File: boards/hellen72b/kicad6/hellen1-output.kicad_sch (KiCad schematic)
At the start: 56 parts

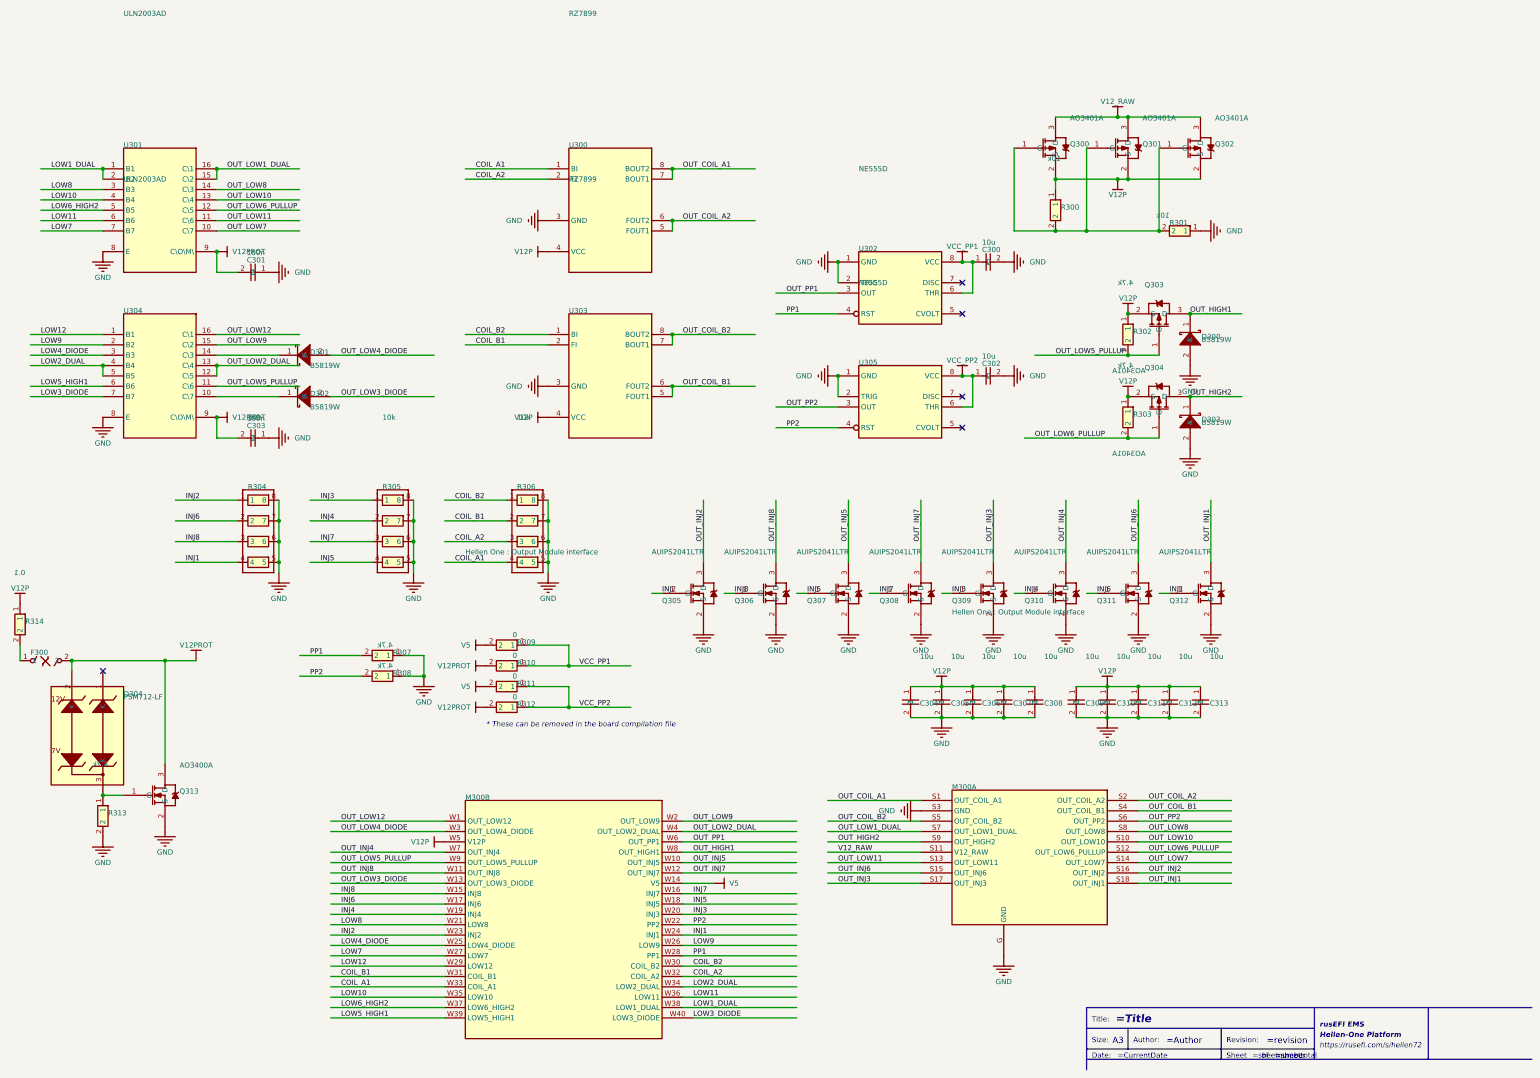
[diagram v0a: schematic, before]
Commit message: update exported kicad files after refactoring
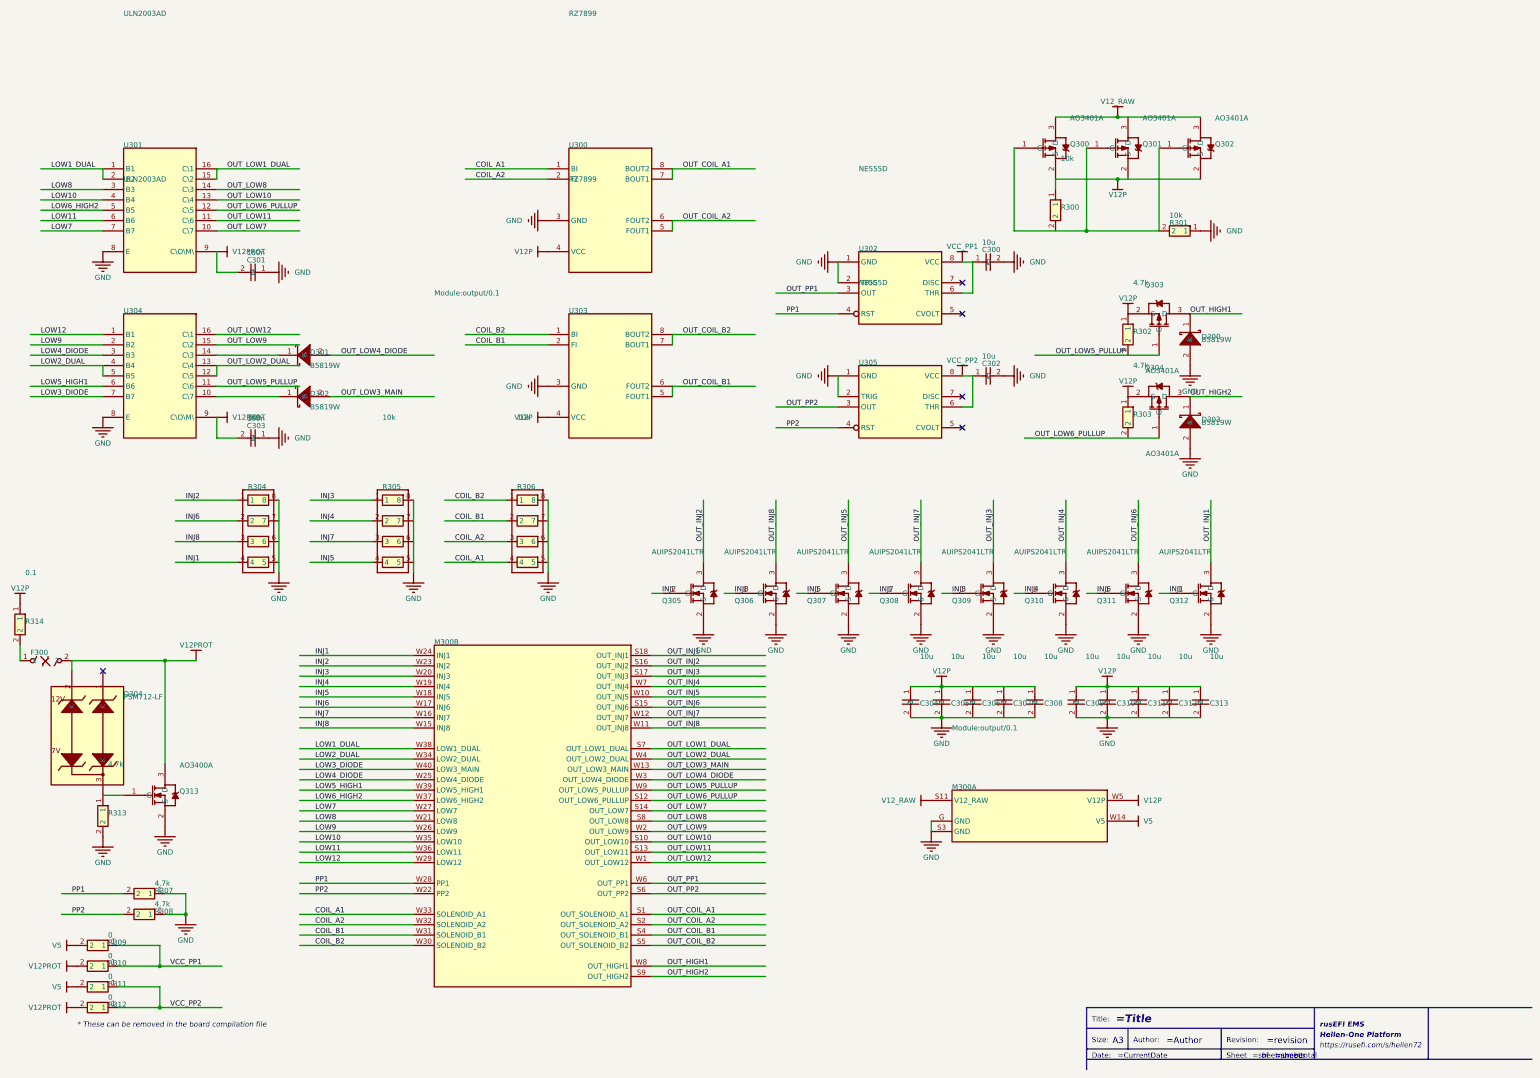
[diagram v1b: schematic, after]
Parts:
- C300, C301, C302, C303, C304, C305, C306, C307, C308, C309, C310, C311, C312, C313, D300, D301, D302, D303, D304, F300, Q300, Q301, Q302, Q303, Q304, Q305, Q306, Q307, Q308, Q309, Q310, Q311, Q312, Q313, R300, R301, R302, R303, R304, R305, R306, R307, R308, R309, R310, R311, R312, R313, R314, U300, U301, U302, U303, U304, U305: value (none) -> ~
- M300: value (none) -> ~; Comment Hellen One : Output Module interface -> Module:output/0.1
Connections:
- net GND: no longer C306.2, C307.2, C311.2, C312.2, R304.5, R304.6, R304.7, R305.5, R305.6, R305.7, R306.5, R306.6, R306.7
- net OUT_COIL_A1: now also M300.S1 (OUT_SOLENOID_A1); no longer M300.S1 (OUT_COIL_A1)
- net OUT_COIL_A2: now also M300.S2 (OUT_SOLENOID_A2); no longer M300.S2 (OUT_COIL_A2)
- net OUT_COIL_B1: now also M300.S4 (OUT_SOLENOID_B1); no longer M300.S4 (OUT_COIL_B1)
- net OUT_COIL_B2: now also M300.S5 (OUT_SOLENOID_B2); no longer M300.S5 (OUT_COIL_B2)
- net OUT_HIGH2: now also M300.S9 (OUT_HIGH2); no longer M300.S9 (OUT_HIGH2)
- net OUT_INJ1: now also M300.S18 (OUT_INJ1); no longer M300.S18 (OUT_INJ1)
- net OUT_INJ2: now also M300.S16 (OUT_INJ2); no longer M300.S16 (OUT_INJ2)
- net OUT_INJ3: now also M300.S17 (OUT_INJ3); no longer M300.S17 (OUT_INJ3)
- net OUT_INJ6: now also M300.S15 (OUT_INJ6); no longer M300.S15 (OUT_INJ6)
- net OUT_LOW10: now also M300.S10 (OUT_LOW10); no longer M300.S10 (OUT_LOW10)
- net OUT_LOW11: now also M300.S13 (OUT_LOW11); no longer M300.S13 (OUT_LOW11)
- net OUT_LOW1_DUAL: now also M300.S7 (OUT_LOW1_DUAL); no longer M300.S7 (OUT_LOW1_DUAL)
- net OUT_LOW5_PULLUP: no longer R302.2
- net OUT_LOW6_PULLUP: now also M300.S12 (OUT_LOW6_PULLUP); no longer M300.S12 (OUT_LOW6_PULLUP), R303.2
- net OUT_LOW7: now also M300.S14 (OUT_LOW7); no longer M300.S14 (OUT_LOW7)
- net OUT_LOW8: now also M300.S8 (OUT_LOW8); no longer M300.S8 (OUT_LOW8)
- net OUT_PP2: now also M300.S6 (OUT_PP2); no longer M300.S6 (OUT_PP2)
- net V12P: now also M300.W5 (V12P); no longer C306.1, C307.1, C311.1, C312.1, M300.W5 (V12P), Q301.2 (S)
- net V12_RAW: no longer Q301.3 (D)
- net V5: now also M300.W14 (V5); no longer M300.W14 (V5)
- net at Q300.1 (G), Q301.1 (G), Q302.1 (G)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: no longer R300.2
- net OUT_LOW3_DIODE renamed OUT_LOW3_MAIN
